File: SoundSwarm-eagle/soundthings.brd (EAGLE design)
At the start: 92.4 x 34.3 mm, 32 parts, among them Q2 MOSFET-NCHANNEL2N7000, Q4 MOSFET-NCHANNEL2N7000, Q5 MOSFET-PCHANNELFQP27P06

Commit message: v2 (to be tested)
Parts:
- removed D2: LED-RGB-CA-THRUCLEAR, SparkFun-LED:LED-RGB-THRU
- removed JP1-SOL, JP2-BAT: (no value), SparkFun-Connectors:JST-2-PTH-VERT
- removed Q5: MOSFET-PCHANNELFQP27P06, SparkFun-DiscreteSemi:TO220V
- added BAT, SOLENOID: (no value), SparkFun-Connectors:JST-2-PTH-VERT
- added LED: LED-RGB-CA-THRUCLEAR, SparkFun-LED:LED-RGB-THRU
- added Q1: IRLIB9343PbF, SparkFun-DiscreteSemi:TO220V
- added R13: 300, SparkFun-Passives:AXIAL-0.3
- D1: value (none) -> 1N4001
- D3: value DIODE-ZENERPTH -> 1N5817; device SparkFun-DiscreteSemi:DIODE-ZENER -> adafruit:DO41-10
- Q2, Q4: value MOSFET-NCHANNEL2N7000 -> IRLB8721PBF; device SparkFun-DiscreteSemi:TO-92 -> SparkFun-DiscreteSemi:TO220V
- R8: value (none) -> 300
- U$2: value TP4057SOT-26-R -> TP4057
- moved GV0RT 10.2 mm to (29.2, 30.5), turned to 0 degrees
- moved U$5 6.48 mm to (14.0, 15.2), flipped to the bottom, turned to 0 degrees
- moved U$2 4.02 mm to (14.0, 20.3), flipped to the bottom, turned to 90 degrees
- moved Q2 2.84 mm to (87.6, 24.1), turned to 270 degrees
- moved D1 2.54 mm to (80.0, 25.4)
- moved D3 1.42 mm to (74.9, 17.1), turned to 90 degrees
- moved C1 1.42 mm to (81.3, 17.1)
- moved Q4 1.27 mm to (87.6, 11.4), turned to 270 degrees
- moved R7 1.27 mm to (17.8, 17.8)
- renumbered JP1-3V3 to 3V3, JP2-ADXL to ADXL
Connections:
- net N$10 renamed 5V
- net N$17 renamed ADC
- net N$4 renamed GPIO16
- removed net N$13: Q4.2, Q5.1, R8.P$1
- new net GATE: Q1.1, Q4.1, R8.P$1
- new net N$4: C1.2, Q1.2, Q4.2, R13.P$2
- net GND: now also BAT.2, Q2.3, Q4.3; no longer JP2-BAT.2, Q2.1, Q4.1
- net N$1: now also Q2.2, SOLENOID.2; no longer JP1-SOL.2, Q2.3
- net N$12: now also Q2.1, R13.P$1; no longer C1.2, Q2.2, Q4.3, Q5.3
- net N$14: now also LED.1; no longer D2.1
- net N$2: now also LED.4; no longer D2.4
- net N$9: now also LED.3; no longer D2.3
- net VBAT: now also BAT.1, D3.A, Q1.3; no longer D3.P$2, JP2-BAT.1, Q5.2
- net VDD: now also LED.2; no longer D2.2
- net VHI: now also D3.C, SOLENOID.1; no longer D3.P$1, JP1-SOL.1
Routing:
- net GATE: track 0.00 -> 52.3 mm
- net N$13: track 48.7 -> 0.00 mm
- net VBAT: track 109.3 -> 146.4 mm, vias 0 -> 1
- net N$4: track 0.00 -> 24.5 mm
- net 3.3V: track 135.2 -> 119.4 mm
- net N$15: track 17.4 -> 7.29 mm
- net GND: track 176.3 -> 167.2 mm, vias 0 -> 1
- net N$16: track 20.0 -> 13.0 mm
- net VDD: track 83.0 -> 78.1 mm, vias 1 -> 0
- net VHI: track 16.6 -> 21.4 mm
- net 5V: track 28.3 -> 32.6 mm
- net N$12: track 23.4 -> 19.9 mm
- net N$11: track 4.80 -> 6.43 mm
- net N$9: track 15.9 -> 15.1 mm
- net N$14: track 15.2 -> 14.6 mm
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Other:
- board size 92.4 x 34.3 mm -> 100 x 34.3 mm
- board text added: "SSv2"
- board text removed: "SSv1"

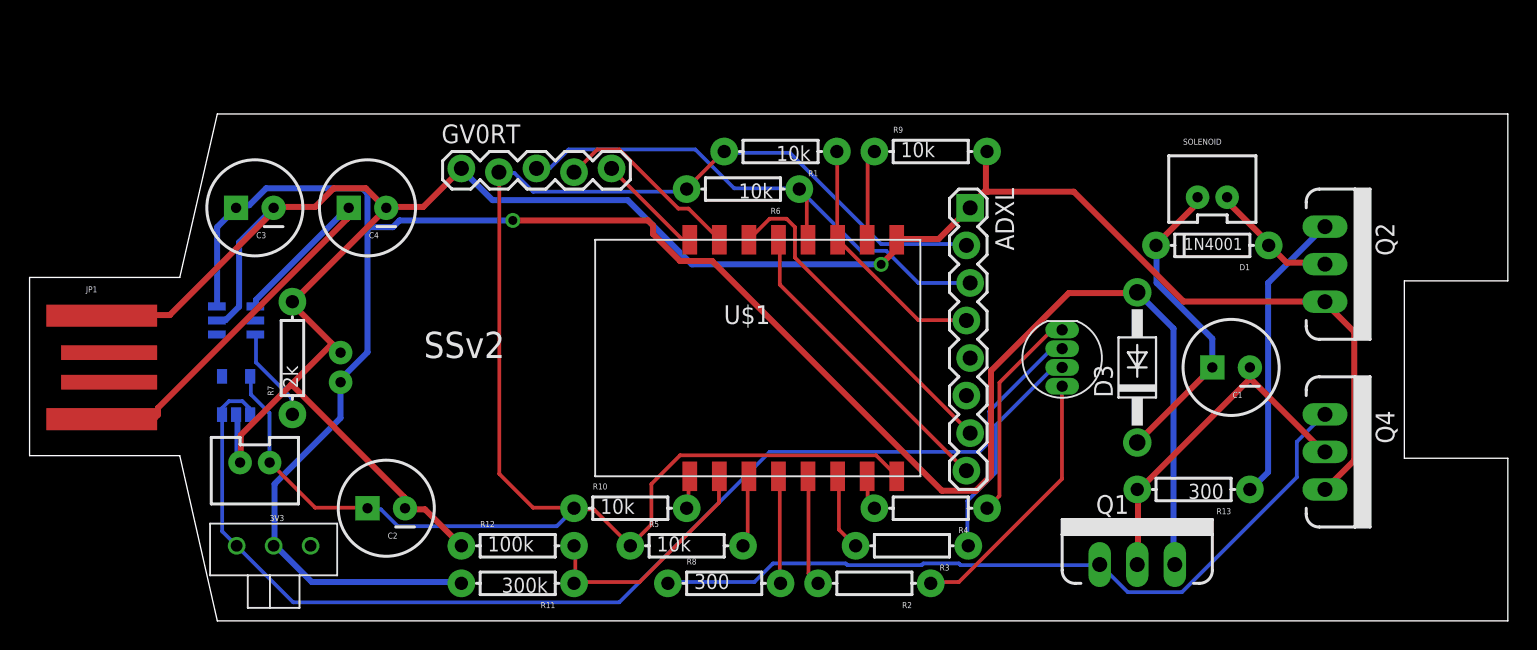
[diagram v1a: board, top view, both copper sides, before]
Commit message: Update board with mounting holes
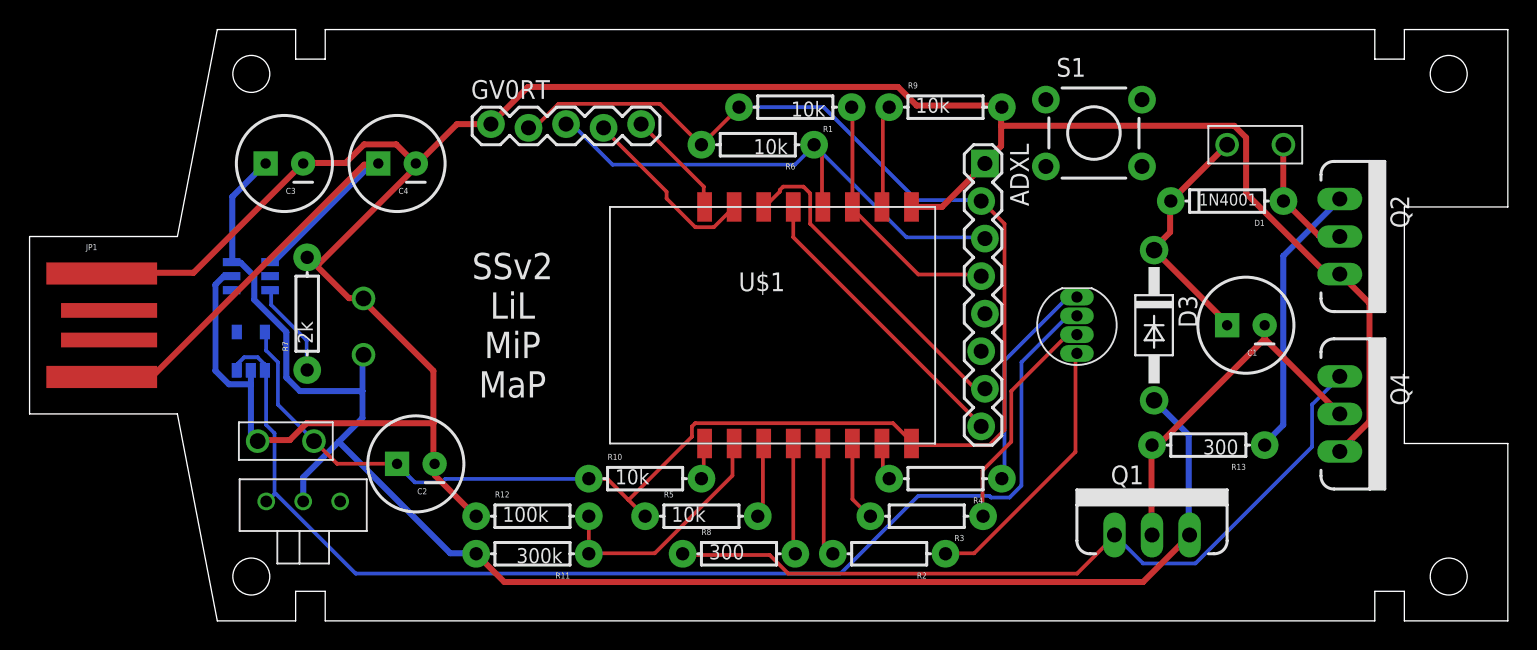
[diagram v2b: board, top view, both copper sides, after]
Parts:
- added S1: SWITCH-MOMENTARY-2PTH, SparkFun-Electromechanical:TACTILE-PTH
- 3V3, BAT, SOLENOID: device SparkFun-Connectors:JST-2-PTH-VERT -> SparkFun-Connectors:1X02_BIG
- moved 3V3 4.47 mm to (19.2, 12.2)
- moved C4 3.61 mm to (24.9, 30.9)
- moved S2 3.61 mm to (18.5, 8.08)
- moved C3 3.61 mm to (17.2, 30.9)
- moved C2 3.61 mm to (26.1, 10.6)
- moved GV0RT 3.61 mm to (31.2, 33.5)
- moved ADXL 3.16 mm to (64.5, 30.9)
- moved D1 3.16 mm to (81.0, 28.4)
- moved R1 3.16 mm to (51.8, 34.8)
- moved R13 3.16 mm to (79.7, 11.9)
- moved R6 3.16 mm to (49.3, 32.2)
- moved R7 3.16 mm to (18.8, 20.8)
- moved R9 3.16 mm to (62.0, 34.8)
- moved SOLENOID 3.16 mm to (81.0, 32.2)
- moved U$2 3.16 mm to (15.0, 23.3)
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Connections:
- net 3.3V: now also 3V3.P$1; no longer 3V3.1
- net GND: now also 3V3.P$2, BAT.P$2; no longer 3V3.2, BAT.2
- net N$1: now also SOLENOID.P$2; no longer SOLENOID.2
- net VBAT: now also BAT.P$1; no longer BAT.1
- net VHI: now also SOLENOID.P$1; no longer SOLENOID.1
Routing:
- net VBAT: track 146.4 -> 107.4 mm, vias 1 -> 0
- net GND: track 167.2 -> 181.8 mm, vias 1 -> 0
- net VHI: track 21.4 -> 16.3 mm
- net 3.3V: track 119.4 -> 114.9 mm
- net VDD: track 78.1 -> 81.2 mm
- net 5V: track 32.6 -> 34.8 mm
- net GATE: track 52.3 -> 53.9 mm
- net N$12: track 19.9 -> 18.7 mm
- net N$19: track 6.17 -> 7.03 mm
- net SCL: track 20.9 -> 20.1 mm
- net INT: track 16.9 -> 17.6 mm
- net N$16: track 13.0 -> 12.5 mm
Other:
- board size 100 x 34.3 mm -> 100 x 40 mm
- board text added: "SSv2 LiL MiP MaP"
- board text removed: "SSv2"
